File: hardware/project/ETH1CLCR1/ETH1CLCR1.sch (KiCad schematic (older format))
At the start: 0 parts

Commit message: Schematic design
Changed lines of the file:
@@
 $Descr A3 16535 11693
 encoding utf-8
-Sheet 1 12
+Sheet 1 13
 Title ""
 Date ""
@@
 F4 "TRIG_OUT" I L 14000 4900 50
 F5 "TRIG_IN" O L 14000 5000 50
-$EndSheet
-$Sheet
-S 9200 3400 1650 6000
-U 5DEACD0F
-F0 "MCU2" 50
-F1 "MCU2.sch" 50
 $EndSheet
 $Sheet
@@
 	7800 8600 7700 8600
 $Sheet
-S 4900 6600 1250 2800
+S 5250 6000 1250 3400
 U 5E314C16
 F0 "FGEN Buffer" 50
 F1 "FGEN_Buffer.sch" 50
+F2 "FGEN" I R 6500 6700 50
+F3 "SR10CTR" I R 6500 6100 50
+F4 "SR100CTR" I R 6500 6200 50
+F5 "SR1KCTR" I R 6500 6300 50
+F6 "SR10KCTR" I R 6500 6400 50
+$EndSheet
+Wire Wire Line
+	6600 6700 6500 6700
+Wire Wire Line
+	6500 6400 9200 6400
+Wire Wire Line
+	6500 6300 9200 6300
+Wire Wire Line
+	6500 6200 9200 6200
+Wire Wire Line
+	6500 6100 9200 6100
+$Sheet
+S 9200 3400 1650 6000
+U 5DEACD0F
+F0 "MCU2" 50
+F1 "MCU2.sch" 50
+F2 "MCU2_~SSS" I R 10850 3800 50
+F3 "MCU2_MISO" O R 10850 3900 50
+F4 "MCU2_MOSI" I R 10850 4000 50
+F5 "MCU2_SCLK" I R 10850 4100 50
+F6 "MCU2_GPIO_OUT1" I R 10850 3700 50
+F7 "MCU2_STATUS_IN" O R 10850 3500 50
+F8 "MCU2_GPIO_OUT2" I R 10850 3600 50
+F9 "MCU3_NSS" O L 9200 7000 50
+F10 "MCU3_SCLK" O L 9200 6700 50
+F11 "MCU3_MISO" I L 9200 6800 50
+F12 "MCU3_MOSI" O L 9200 6900 50
+F13 "SR1KCTR" O L 9200 6300 50
+F14 "SR10KCTR" O L 9200 6400 50
+F15 "SR10CTR" O L 9200 6100 50
+F16 "SR100CTR" O L 9200 6200 50
+$EndSheet
+Wire Wire Line
+	7700 8400 7800 8400
+Wire Wire Line
+	7700 8300 7800 8300
+Wire Wire Line
+	7700 8200 7800 8200
+Wire Wire Line
+	7800 8100 7700 8100
+Wire Wire Line
+	7700 8000 7800 8000
+Wire Wire Line
+	7800 7900 7700 7900
+Wire Wire Line
+	7700 7800 7800 7800
+Wire Wire Line
+	7700 7600 7800 7600
+Wire Wire Line
+	7800 7500 7700 7500
+Wire Wire Line
+	7700 7400 7800 7400
+Wire Wire Line
+	7800 7300 7700 7300
+Wire Wire Line
+	7700 7200 7800 7200
+Wire Wire Line
+	7800 7100 7700 7100
+Wire Wire Line
+	7700 6900 7800 6900
+Wire Wire Line
+	7800 6800 7700 6800
+Wire Wire Line
+	7700 6700 7800 6700
+$Sheet
+S 3800 6000 1250 3400
+U 5E252C19
+F0 "Range Resistors" 50
+F1 "RangeResistor.sch" 50
 $EndSheet
 $EndSCHEMATC

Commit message: Schematic design
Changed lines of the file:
@@
 $Descr A3 16535 11693
 encoding utf-8
-Sheet 1 13
+Sheet 1 14
 Title ""
 Date ""
@@
 	7700 6700 7800 6700
 $Sheet
-S 3800 6000 1250 3400
+S 3200 6000 1250 3400
 U 5E252C19
 F0 "Range Resistors" 50
 F1 "RangeResistor.sch" 50
+F2 "R1KCRT" I R 4450 6350 50
+F3 "R10KCRT" I R 4450 6450 50
+F4 "R100CRT" I R 4450 6250 50
+F5 "R10CRT" I R 4450 6150 50
+F6 "R100KCRT" I R 4450 6550 50
+F7 "Err" O L 3200 6150 50
+$EndSheet
+Wire Wire Line
+	9100 6700 9200 6700
+Wire Wire Line
+	9200 6800 9100 6800
+Wire Wire Line
+	9100 6900 9200 6900
+Wire Wire Line
+	9200 7000 9100 7000
+$Sheet
+S 1850 5900 1000 2200
+U 5EB3D8D6
+F0 "Process Amplifier" 50
+F1 "ProcessAmplifier.sch" 50
 $EndSheet
 $EndSCHEMATC

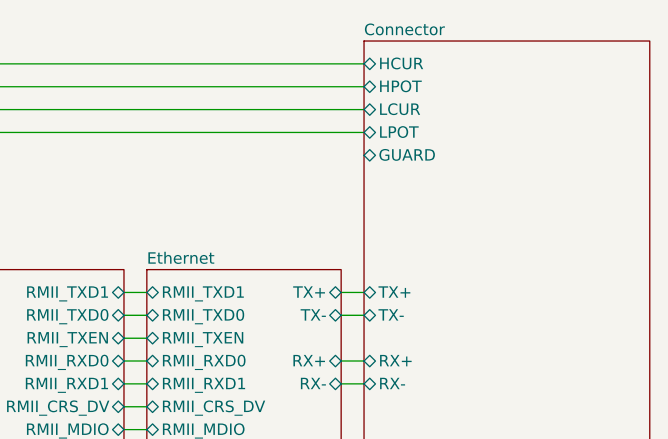
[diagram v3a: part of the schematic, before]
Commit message: Need to redesign the AC source, the LT1468 is too slow.
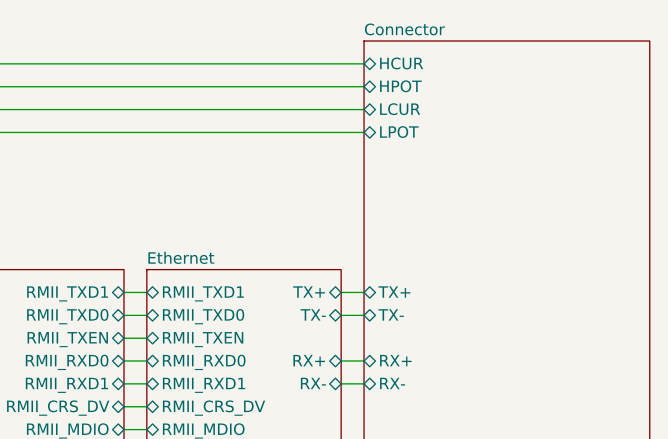
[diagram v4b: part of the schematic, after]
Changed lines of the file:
@@
 F9 "LCUR" B L 14600 950 50
 F10 "LPOT" B L 14600 1050 50
-F11 "GUARD" B L 14600 1150 50
-F12 "CXN_RELA" I L 14600 5000 50
-F13 "CXN_RELB" I L 14600 5100 50
-F14 "CXN_RELC" I L 14600 5200 50
-F15 "CXN_RELD" I L 14600 5300 50
-F16 "CXN_RELE" I L 14600 5400 50
-F17 "CXN_RELF" I L 14600 5500 50
+F11 "CXN_RELA" I L 14600 5000 50
+F12 "CXN_RELB" I L 14600 5100 50
+F13 "CXN_RELC" I L 14600 5200 50
+F14 "CXN_RELD" I L 14600 5300 50
+F15 "CXN_RELE" I L 14600 5400 50
+F16 "CXN_RELF" I L 14600 5500 50
 $EndSheet
 Wire Wire Line

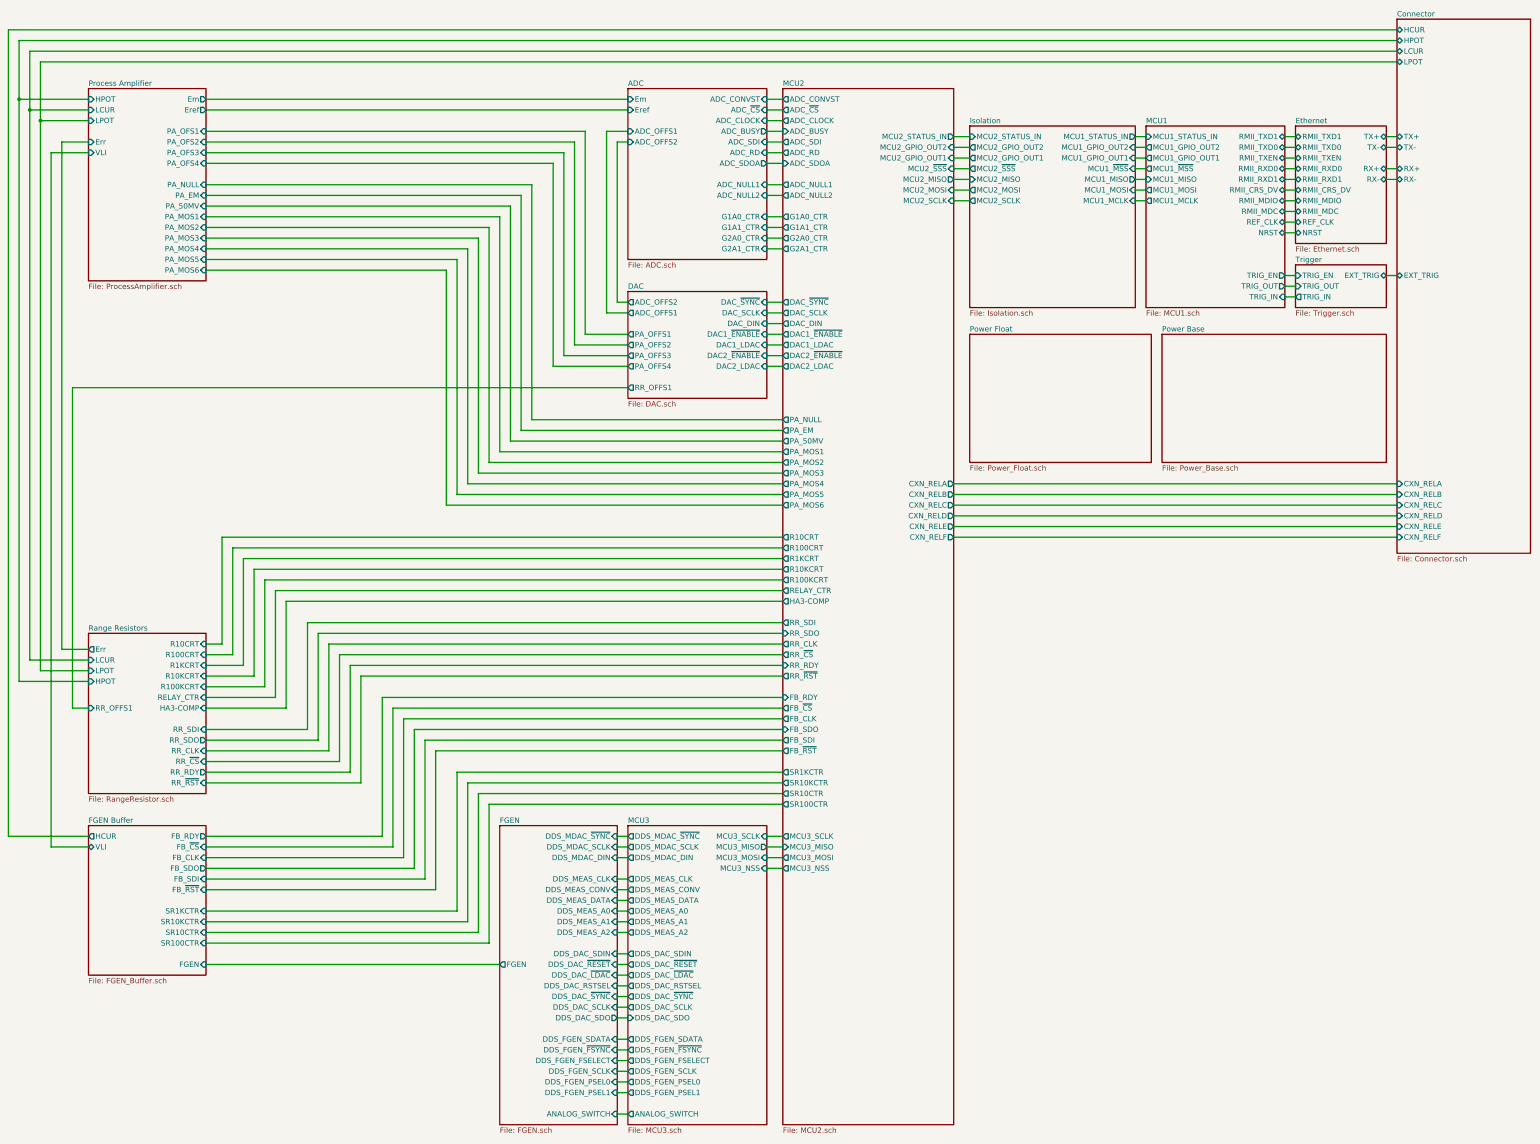
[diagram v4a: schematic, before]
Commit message: Footprint asigment (not finished).
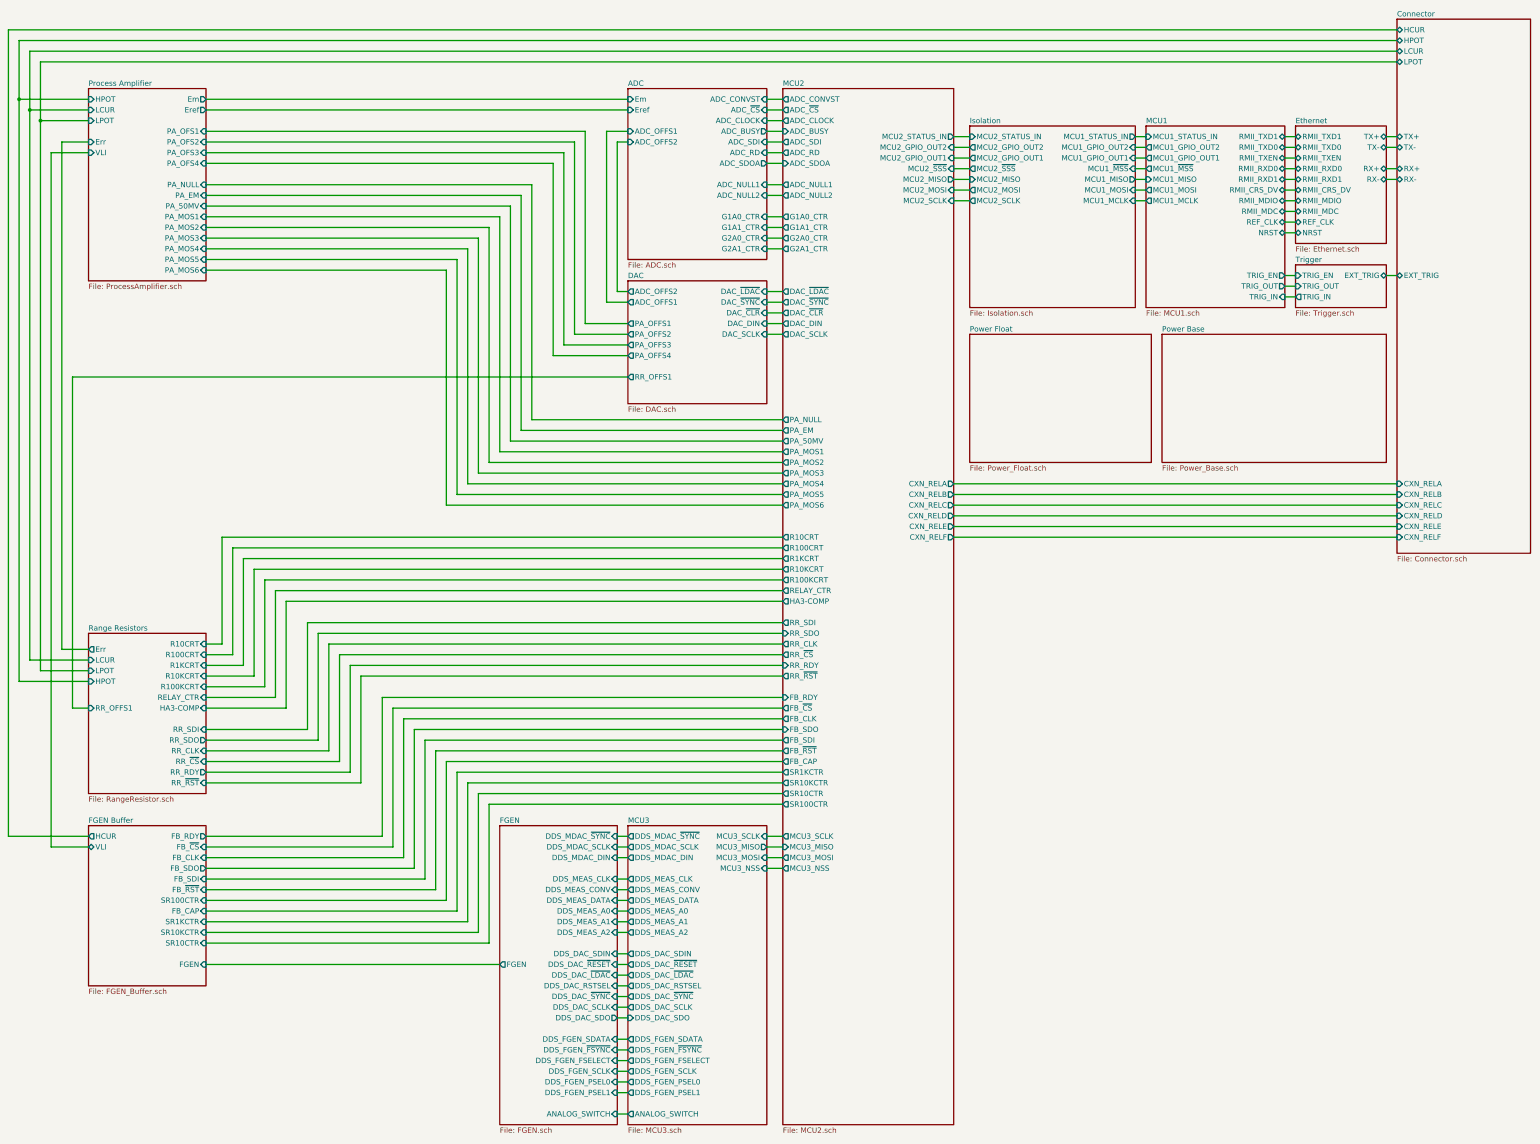
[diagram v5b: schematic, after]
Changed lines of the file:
@@
 	7400 10200 7300 10200
 $Sheet
-S 2350 8200 1100 1400
+S 2350 8200 1100 1500
 U 5E314C16
 F0 "FGEN Buffer" 50
 F1 "FGEN_Buffer.sch" 50
 F2 "FGEN" I R 3450 9500 50
-F3 "SR10CTR" I R 3450 9200 50
-F4 "SR100CTR" I R 3450 9300 50
-F5 "SR1KCTR" I R 3450 9000 50
-F6 "SR10KCTR" I R 3450 9100 50
+F3 "SR10CTR" I R 3450 9300 50
+F4 "SR100CTR" I R 3450 8900 50
+F5 "SR1KCTR" I R 3450 9100 50
+F6 "SR10KCTR" I R 3450 9200 50
 F7 "VLI" B L 2350 8400 50
 F8 "HCUR" O L 2350 8300 50
@@
 F13 "FB_RDY" O R 3450 8300 50
 F14 "FB_~RST" I R 3450 8800 50
+F15 "FB_CAP" I R 3450 9000 50
 $EndSheet
 $Sheet
@@
 F37 "PA_MOS5" O L 8850 5100 50
 F38 "PA_MOS6" O L 8850 5200 50
-F39 "DAC_~SYNC" O L 8850 3300 50
-F40 "DAC_SCLK" O L 8850 3400 50
-F41 "DAC_DIN" O L 8850 3500 50
-F42 "DAC1_~ENABLE" O L 8850 3600 50
-F43 "DAC1_LDAC" O L 8850 3700 50
-F44 "DAC2_~ENABLE" O L 8850 3800 50
-F45 "DAC2_LDAC" O L 8850 3900 50
-F46 "G1A1_CTR" O L 8850 2600 50
-F47 "G1A0_CTR" O L 8850 2500 50
-F48 "G2A1_CTR" O L 8850 2800 50
-F49 "G2A0_CTR" O L 8850 2700 50
-F50 "ADC_NULL2" O L 8850 2300 50
-F51 "ADC_NULL1" O L 8850 2200 50
-F52 "ADC_CONVST" O L 8850 1400 50
-F53 "ADC_~CS" O L 8850 1500 50
-F54 "ADC_CLOCK" O L 8850 1600 50
-F55 "ADC_BUSY" I L 8850 1700 50
-F56 "ADC_SDI" O L 8850 1800 50
-F57 "ADC_RD" O L 8850 1900 50
-F58 "ADC_SDOA" I L 8850 2000 50
-F59 "RR_SDI" O L 8850 6300 50
-F60 "RR_SDO" I L 8850 6400 50
-F61 "RR_CLK" O L 8850 6500 50
-F62 "RR_~CS" O L 8850 6600 50
-F63 "RR_RDY" I L 8850 6700 50
-F64 "RR_~RST" O L 8850 6800 50
-F65 "FB_SDI" O L 8850 7400 50
-F66 "FB_SDO" I L 8850 7300 50
-F67 "FB_CLK" O L 8850 7200 50
-F68 "FB_~CS" O L 8850 7100 50
-F69 "FB_RDY" I L 8850 7000 50
-F70 "FB_~RST" O L 8850 7500 50
+F39 "G1A1_CTR" O L 8850 2600 50
+F40 "G1A0_CTR" O L 8850 2500 50
+F41 "G2A1_CTR" O L 8850 2800 50
+F42 "G2A0_CTR" O L 8850 2700 50
+F43 "ADC_NULL2" O L 8850 2300 50
+F44 "ADC_NULL1" O L 8850 2200 50
+F45 "ADC_CONVST" O L 8850 1400 50
+F46 "ADC_~CS" O L 8850 1500 50
+F47 "ADC_CLOCK" O L 8850 1600 50
+F48 "ADC_BUSY" I L 8850 1700 50
+F49 "ADC_SDI" O L 8850 1800 50
+F50 "ADC_RD" O L 8850 1900 50
+F51 "ADC_SDOA" I L 8850 2000 50
+F52 "RR_SDI" O L 8850 6300 50
+F53 "RR_SDO" I L 8850 6400 50
+F54 "RR_CLK" O L 8850 6500 50
+F55 "RR_~CS" O L 8850 6600 50
+F56 "RR_RDY" I L 8850 6700 50
+F57 "RR_~RST" O L 8850 6800 50
+F58 "FB_SDI" O L 8850 7400 50
+F59 "FB_SDO" I L 8850 7300 50
+F60 "FB_CLK" O L 8850 7200 50
+F61 "FB_~CS" O L 8850 7100 50
+F62 "FB_RDY" I L 8850 7000 50
+F63 "FB_~RST" O L 8850 7500 50
+F64 "DAC_~LDAC" O L 8850 3200 50
+F65 "DAC_~SYNC" O L 8850 3300 50
+F66 "DAC_~CLR" O L 8850 3400 50
+F67 "DAC_DIN" O L 8850 3500 50
+F68 "DAC_SCLK" O L 8850 3600 50
+F69 "FB_CAP" O L 8850 7600 50
 $EndSheet
 Wire Wire Line
@@
 $EndSheet
 $Sheet
-S 7400 3200 1300 1000
+S 7400 3100 1300 1150
 U 5E087FDC
 F0 "DAC" 50
 F1 "DAC.sch" 50
-F2 "PA_OFFS1" O L 7400 3600 50
-F3 "PA_OFFS2" O L 7400 3700 50
-F4 "PA_OFFS3" O L 7400 3800 50
-F5 "PA_OFFS4" O L 7400 3900 50
-F6 "DAC_~SYNC" I R 8700 3300 50
-F7 "DAC_SCLK" I R 8700 3400 50
-F8 "DAC_DIN" I R 8700 3500 50
-F9 "DAC1_~ENABLE" I R 8700 3600 50
-F10 "DAC1_LDAC" I R 8700 3700 50
-F11 "ADC_OFFS1" O L 7400 3400 50
-F12 "ADC_OFFS2" O L 7400 3300 50
-F13 "DAC2_~ENABLE" I R 8700 3800 50
-F14 "DAC2_LDAC" I R 8700 3900 50
-F15 "RR_OFFS1" O L 7400 4100 50
+F2 "PA_OFFS1" O L 7400 3500 50
+F3 "PA_OFFS2" O L 7400 3600 50
+F4 "PA_OFFS3" O L 7400 3700 50
+F5 "PA_OFFS4" O L 7400 3800 50
+F6 "ADC_OFFS1" O L 7400 3300 50
+F7 "ADC_OFFS2" O L 7400 3200 50
+F8 "RR_OFFS1" O L 7400 4000 50
+F9 "DAC_~LDAC" I R 8700 3200 50
+F10 "DAC_~SYNC" I R 8700 3300 50
+F11 "DAC_~CLR" I R 8700 3400 50
+F12 "DAC_DIN" I R 8700 3500 50
+F13 "DAC_SCLK" I R 8700 3600 50
 $EndSheet
 $Sheet
@@
 	14600 5500 10450 5500
 Wire Wire Line
-	7400 3300 7300 3300
-Wire Wire Line
-	7300 3300 7300 1800
+	7400 3200 7300 3200
+Wire Wire Line
+	7300 3200 7300 1800
 Wire Wire Line
 	7300 1800 7400 1800
 Wire Wire Line
-	7400 3400 7200 3400
-Wire Wire Line
-	7200 3400 7200 1700
+	7400 3300 7200 3300
+Wire Wire Line
+	7200 3300 7200 1700
 Wire Wire Line
 	7200 1700 7400 1700
@@
 	3450 1700 7000 1700
 Wire Wire Line
-	7000 1700 7000 3600
-Wire Wire Line
-	7000 3600 7400 3600
+	7000 1700 7000 3500
+Wire Wire Line
+	7000 3500 7400 3500
 Wire Wire Line
 	3450 1800 6900 1800
 Wire Wire Line
-	6900 1800 6900 3700
-Wire Wire Line
-	6900 3700 7400 3700
+	6900 1800 6900 3600
+Wire Wire Line
+	6900 3600 7400 3600
 Wire Wire Line
 	3450 1900 6800 1900
 Wire Wire Line
-	6800 1900 6800 3800
-Wire Wire Line
-	6800 3800 7400 3800
+	6800 1900 6800 3700
+Wire Wire Line
+	6800 3700 7400 3700
 Wire Wire Line
 	3450 2000 6700 2000
 Wire Wire Line
-	6700 2000 6700 3900
-Wire Wire Line
-	6700 3900 7400 3900
+	6700 2000 6700 3800
+Wire Wire Line
+	6700 3800 7400 3800
 Wire Wire Line
 	3450 1500 7400 1500
@@
 	2350 7100 2200 7100
 Wire Wire Line
-	2200 7100 2200 4100
-Wire Wire Line
-	2200 4100 7400 4100
+	2200 7100 2200 4000
+Wire Wire Line
+	2200 4000 7400 4000
 Wire Wire Line
 	8700 1400 8850 1400
@@
 	8700 2800 8850 2800
 Wire Wire Line
+	10450 2350 10600 2350
+Wire Wire Line
+	10600 2250 10450 2250
+Wire Wire Line
+	10450 2150 10600 2150
+Wire Wire Line
+	10600 2050 10450 2050
+Wire Wire Line
+	10450 1950 10600 1950
+Wire Wire Line
+	10600 1850 10450 1850
+Wire Wire Line
+	10450 1750 10600 1750
+Wire Wire Line
+	3450 8900 5700 8900
+Wire Wire Line
+	5700 8900 5700 7600
+Wire Wire Line
+	5700 7600 8850 7600
+Wire Wire Line
+	8850 3200 8700 3200
+Wire Wire Line
 	8700 3300 8850 3300
 Wire Wire Line
-	8700 3400 8850 3400
+	8850 3400 8700 3400
 Wire Wire Line
 	8700 3500 8850 3500
 Wire Wire Line
-	8700 3600 8850 3600
-Wire Wire Line
-	8700 3700 8850 3700
-Wire Wire Line
-	8700 3800 8850 3800
-Wire Wire Line
-	8700 3900 8850 3900
-Wire Wire Line
-	10450 2350 10600 2350
-Wire Wire Line
-	10600 2250 10450 2250
-Wire Wire Line
-	10450 2150 10600 2150
-Wire Wire Line
-	10600 2050 10450 2050
-Wire Wire Line
-	10450 1950 10600 1950
-Wire Wire Line
-	10600 1850 10450 1850
-Wire Wire Line
-	10450 1750 10600 1750
+	8850 3600 8700 3600
 $EndSCHEMATC

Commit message: Modification in schematic and PCB layout.
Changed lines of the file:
@@
 F15 "SR10CTR" O L 8850 7900 50
 F16 "SR100CTR" O L 8850 8000 50
-F17 "CXN_RELA" O R 10450 5000 50
-F18 "CXN_RELB" O R 10450 5100 50
-F19 "CXN_RELC" O R 10450 5200 50
-F20 "CXN_RELD" O R 10450 5300 50
-F21 "CXN_RELE" O R 10450 5400 50
-F22 "CXN_RELF" O R 10450 5500 50
-F23 "R100CRT" O L 8850 5600 50
-F24 "R10CRT" O L 8850 5500 50
-F25 "R1KCRT" O L 8850 5700 50
-F26 "R10KCRT" O L 8850 5800 50
-F27 "R100KCRT" O L 8850 5900 50
-F28 "RELAY_CTR" O L 8850 6000 50
-F29 "HA3-COMP" O L 8850 6100 50
-F30 "PA_NULL" O L 8850 4400 50
-F31 "PA_EM" O L 8850 4500 50
-F32 "PA_50MV" O L 8850 4600 50
-F33 "PA_MOS1" O L 8850 4700 50
-F34 "PA_MOS2" O L 8850 4800 50
-F35 "PA_MOS3" O L 8850 4900 50
-F36 "PA_MOS4" O L 8850 5000 50
-F37 "PA_MOS5" O L 8850 5100 50
-F38 "PA_MOS6" O L 8850 5200 50
-F39 "G1A1_CTR" O L 8850 2600 50
-F40 "G1A0_CTR" O L 8850 2500 50
-F41 "G2A1_CTR" O L 8850 2800 50
-F42 "G2A0_CTR" O L 8850 2700 50
-F43 "ADC_NULL2" O L 8850 2300 50
-F44 "ADC_NULL1" O L 8850 2200 50
-F45 "ADC_CONVST" O L 8850 1400 50
-F46 "ADC_~CS" O L 8850 1500 50
-F47 "ADC_CLOCK" O L 8850 1600 50
-F48 "ADC_BUSY" I L 8850 1700 50
-F49 "ADC_SDI" O L 8850 1800 50
-F50 "ADC_RD" O L 8850 1900 50
-F51 "ADC_SDOA" I L 8850 2000 50
-F52 "RR_SDI" O L 8850 6300 50
-F53 "RR_SDO" I L 8850 6400 50
-F54 "RR_CLK" O L 8850 6500 50
-F55 "RR_~CS" O L 8850 6600 50
-F56 "RR_RDY" I L 8850 6700 50
-F57 "RR_~RST" O L 8850 6800 50
-F58 "FB_SDI" O L 8850 7400 50
-F59 "FB_SDO" I L 8850 7300 50
-F60 "FB_CLK" O L 8850 7200 50
-F61 "FB_~CS" O L 8850 7100 50
-F62 "FB_RDY" I L 8850 7000 50
-F63 "FB_~RST" O L 8850 7500 50
-F64 "DAC_~LDAC" O L 8850 3200 50
-F65 "DAC_~SYNC" O L 8850 3300 50
-F66 "DAC_~CLR" O L 8850 3400 50
-F67 "DAC_DIN" O L 8850 3500 50
-F68 "DAC_SCLK" O L 8850 3600 50
-F69 "FB_CAP" O L 8850 7600 50
+F17 "CXN_REL1" O R 10450 5000 50
+F18 "CXN_REL2" O R 10450 5100 50
+F19 "CXN_REL3" O R 10450 5200 50
+F20 "R100CRT" O L 8850 5600 50
+F21 "R10CRT" O L 8850 5500 50
+F22 "R1KCRT" O L 8850 5700 50
+F23 "R10KCRT" O L 8850 5800 50
+F24 "R100KCRT" O L 8850 5900 50
+F25 "RELAY_CTR" O L 8850 6000 50
+F26 "HA3-COMP" O L 8850 6100 50
+F27 "PA_NULL" O L 8850 4400 50
+F28 "PA_EM" O L 8850 4500 50
+F29 "PA_50MV" O L 8850 4600 50
+F30 "PA_MOS1" O L 8850 4700 50
+F31 "PA_MOS2" O L 8850 4800 50
+F32 "PA_MOS3" O L 8850 4900 50
+F33 "PA_MOS4" O L 8850 5000 50
+F34 "PA_MOS5" O L 8850 5100 50
+F35 "PA_MOS6" O L 8850 5200 50
+F36 "G1A1_CTR" O L 8850 2600 50
+F37 "G1A0_CTR" O L 8850 2500 50
+F38 "G2A1_CTR" O L 8850 2800 50
+F39 "G2A0_CTR" O L 8850 2700 50
+F40 "ADC_NULL2" O L 8850 2300 50
+F41 "ADC_NULL1" O L 8850 2200 50
+F42 "ADC_CONVST" O L 8850 1400 50
+F43 "ADC_~CS" O L 8850 1500 50
+F44 "ADC_CLOCK" O L 8850 1600 50
+F45 "ADC_BUSY" I L 8850 1700 50
+F46 "ADC_SDI" O L 8850 1800 50
+F47 "ADC_RD" O L 8850 1900 50
+F48 "ADC_SDOA" I L 8850 2000 50
+F49 "RR_SDI" O L 8850 6300 50
+F50 "RR_SDO" I L 8850 6400 50
+F51 "RR_CLK" O L 8850 6500 50
+F52 "RR_~CS" O L 8850 6600 50
+F53 "RR_RDY" I L 8850 6700 50
+F54 "RR_~RST" O L 8850 6800 50
+F55 "FB_SDI" O L 8850 7400 50
+F56 "FB_SDO" I L 8850 7300 50
+F57 "FB_CLK" O L 8850 7200 50
+F58 "FB_~CS" O L 8850 7100 50
+F59 "FB_RDY" I L 8850 7000 50
+F60 "FB_~RST" O L 8850 7500 50
+F61 "DAC_~LDAC" O L 8850 3200 50
+F62 "DAC_~SYNC" O L 8850 3300 50
+F63 "DAC_~CLR" O L 8850 3400 50
+F64 "DAC_DIN" O L 8850 3500 50
+F65 "DAC_SCLK" O L 8850 3600 50
+F66 "FB_CAP" O L 8850 7600 50
+F67 "CXN_REL4" O R 10450 5300 50
+F68 "CXN_REL5" O R 10450 5400 50
+F69 "CXN_REL6" O R 10450 5500 50
 $EndSheet
 Wire Wire Line
@@
 	5500 7400 8850 7400
 $Sheet
-S 14600 650  1250 5000
+S 14600 650  1250 4950
 U 5DEACCC1
 F0 "Connector" 50
@@
 F9 "LCUR" B L 14600 950 50
 F10 "LPOT" B L 14600 1050 50
-F11 "CXN_RELA" I L 14600 5000 50
-F12 "CXN_RELB" I L 14600 5100 50
-F13 "CXN_RELC" I L 14600 5200 50
-F14 "CXN_RELD" I L 14600 5300 50
-F15 "CXN_RELE" I L 14600 5400 50
-F16 "CXN_RELF" I L 14600 5500 50
+F11 "CXN_REL1" I L 14600 5000 50
+F12 "CXN_REL2" I L 14600 5100 50
+F13 "CXN_REL3" I L 14600 5200 50
+F14 "CXN_REL4" I L 14600 5300 50
+F15 "CXN_REL5" I L 14600 5400 50
+F16 "CXN_REL6" I L 14600 5500 50
 $EndSheet
 Wire Wire Line
@@
 Wire Wire Line
 	14600 5200 10450 5200
-Wire Wire Line
-	14600 5300 10450 5300
-Wire Wire Line
-	14600 5400 10450 5400
-Wire Wire Line
-	14600 5500 10450 5500
 Wire Wire Line
 	7400 3200 7300 3200
@@
 Wire Wire Line
 	8850 3600 8700 3600
+Wire Wire Line
+	10450 5300 14600 5300
+Wire Wire Line
+	14600 5400 10450 5400
+Wire Wire Line
+	10450 5500 14600 5500
 $EndSCHEMATC
